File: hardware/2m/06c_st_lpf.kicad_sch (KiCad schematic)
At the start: 10 parts

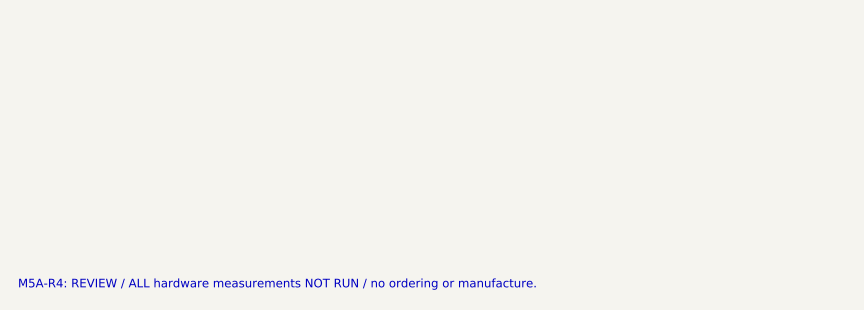
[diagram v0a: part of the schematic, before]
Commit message: Preserve M5B-E1 integrated RF2M evaluation baseline
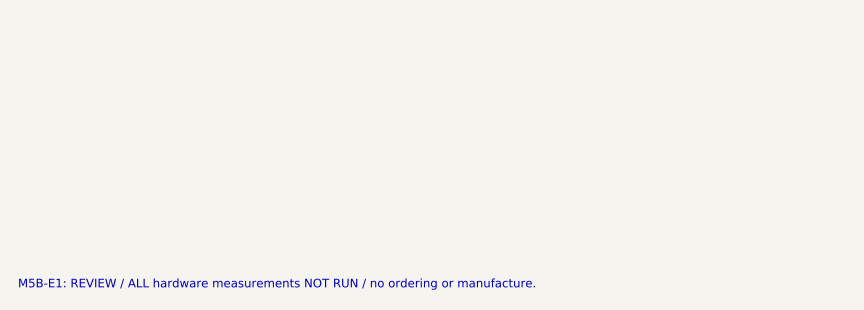
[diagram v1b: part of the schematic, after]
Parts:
- L641, L642, L643: footprint Inductor_SMD:L_1008_2520Metric -> ARDF_2M:Coilcraft_1008CS_Doc101; Engineering_Note Original ST RF value/function. Exact manufacturer land/current stock OPEN; tune/validate on the ONE integrated transmitter. Not an ordinary power inductor. -> Original ST RF value/function. Exact manufacturer land/current stock OPEN; tune/validate on the ONE integrated transmitter. Not an ordinary power inductor. M5B actualDoc101-1 land H2.54 I1.02 J1.27mm;body2.92x2.79,H2.03+.152solder. Values unchanged;1A rise-current,not measured RF RMS margin.
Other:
- note added: "M5B-E1: REVIEW / ALL hardware measurements NOT RUN / no ordering or manufacture."
- note removed: "M5A-R4: REVIEW / ALL hardware measurements NOT RUN / no ordering or manufacture."

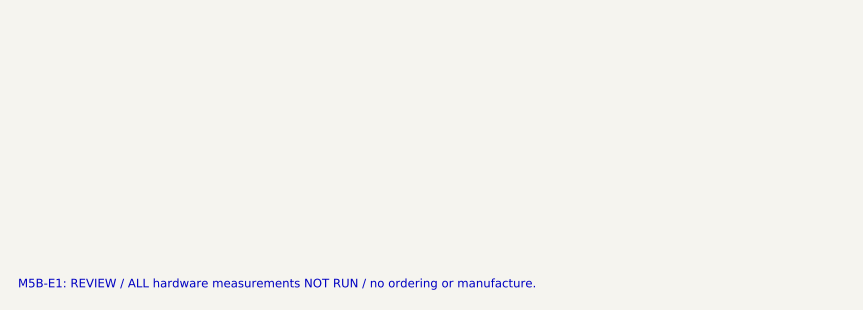
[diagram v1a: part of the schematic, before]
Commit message: Implement M5B-E3 standard JLCPCB RF2M evaluation board
Recalculate and implement 1.6 mm / 1 oz RF geometry, power copper, thermal vias, connector holes and manufacturing legend. Preserve electrical functions and population variants. Add native-geometry DFM, regression checks and fresh native/fabrication review archives. CAD milestone only; no manufacturing or operational release.
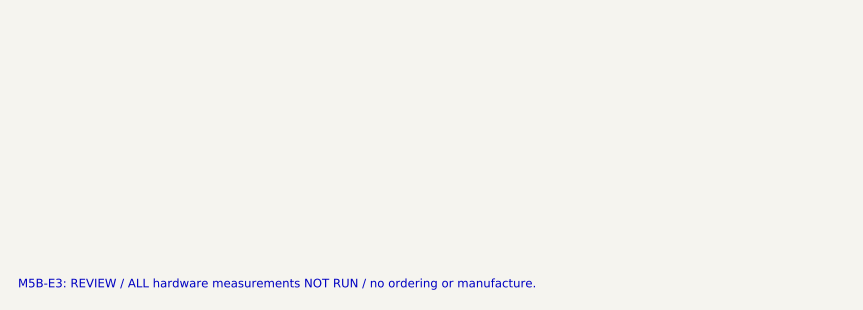
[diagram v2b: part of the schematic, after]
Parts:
- C641, C642, C643, C644, C645, C646, C647: footprint Capacitor_SMD:C_0603_1608Metric -> ARDF_2M:C_0603_1608Metric_E3
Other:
- note added: "M5B-E3: REVIEW / ALL hardware measurements NOT RUN / no ordering or manufacture."
- note removed: "M5B-E1: REVIEW / ALL hardware measurements NOT RUN / no ordering or manufacture."

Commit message: Implement M5B-E4 thermal candidate with source-joint assembly hold
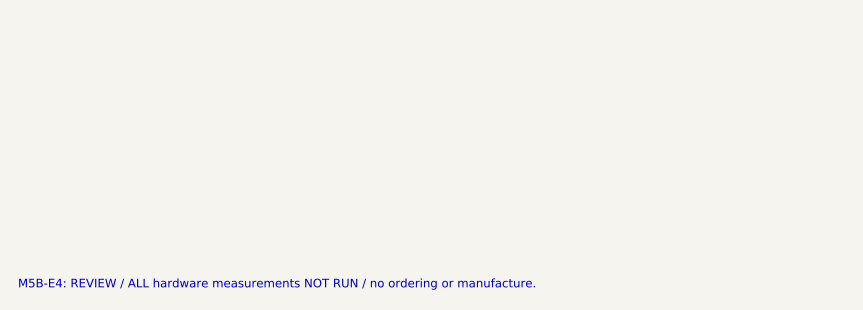
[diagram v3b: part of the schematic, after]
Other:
- note added: "M5B-E4: REVIEW / ALL hardware measurements NOT RUN / no ordering or manufacture."
- note removed: "M5B-E3: REVIEW / ALL hardware measurements NOT RUN / no ordering or manufacture."

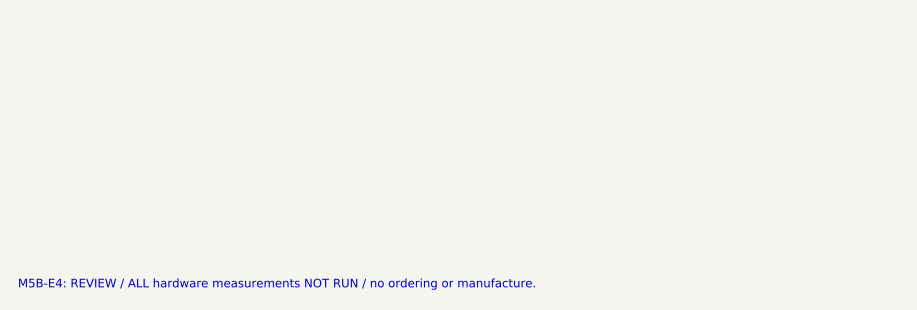
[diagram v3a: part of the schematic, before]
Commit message: Implement M5B-E4R1 source-joint prototype candidate
Replace source mask islands with a controlled open-via hybrid and native-derived local stencil. Preserve standard JLCPCB and RF circuitry. Add assembly qualification, thermal convergence and adverse sensitivities, native DFM/mutation checks and fresh review exports. Conservative 110 C target is missed; 125 C physical gate stays open. No acceptance tag or manufacturing authorization.
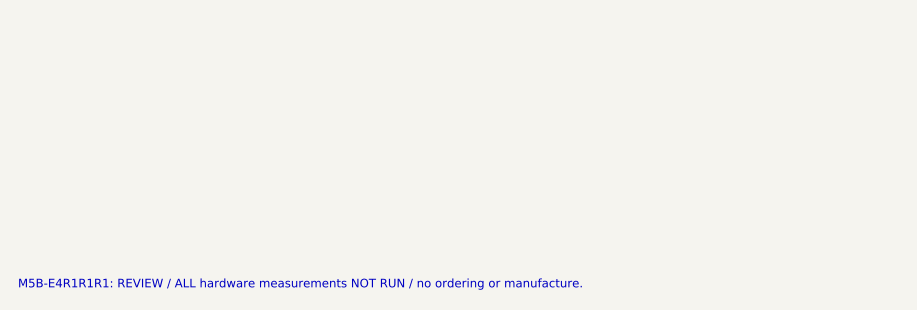
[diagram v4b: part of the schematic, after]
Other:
- note added: "M5B-E4R1R1R1: REVIEW / ALL hardware measurements NOT RUN / no ordering or manufacture."
- note removed: "M5B-E4: REVIEW / ALL hardware measurements NOT RUN / no ordering or manufacture."

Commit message: M5B-E5: compact RF2M to the shared 150x110 mm platform
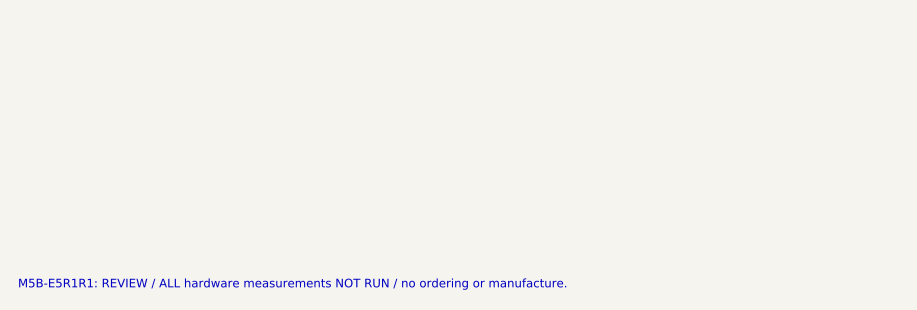
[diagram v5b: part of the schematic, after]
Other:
- note added: "M5B-E5R1R1: REVIEW / ALL hardware measurements NOT RUN / no ordering or manufacture."
- note removed: "M5B-E4R1R1R1: REVIEW / ALL hardware measurements NOT RUN / no ordering or manufacture."

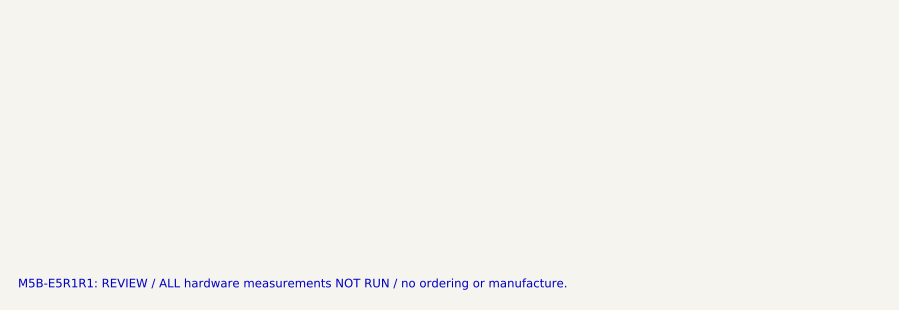
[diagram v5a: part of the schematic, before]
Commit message: M5B-E6R2: Implement carrier-keyed RF2M and unified cooling
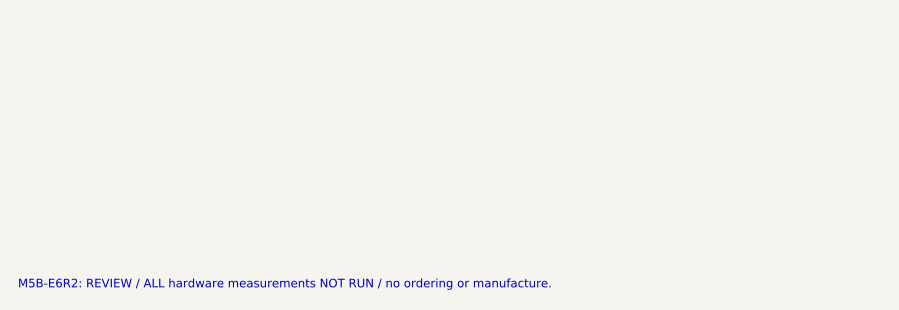
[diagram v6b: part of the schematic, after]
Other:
- note added: "M5B-E6R2: REVIEW / ALL hardware measurements NOT RUN / no ordering or manufacture."
- note removed: "M5B-E5R1R1: REVIEW / ALL hardware measurements NOT RUN / no ordering or manufacture."
